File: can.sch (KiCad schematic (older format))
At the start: 13 parts, among them P7 CAN, U10 MCP2551-I/SN, U11 MCP2515, U12 SG-210STF_16MHz

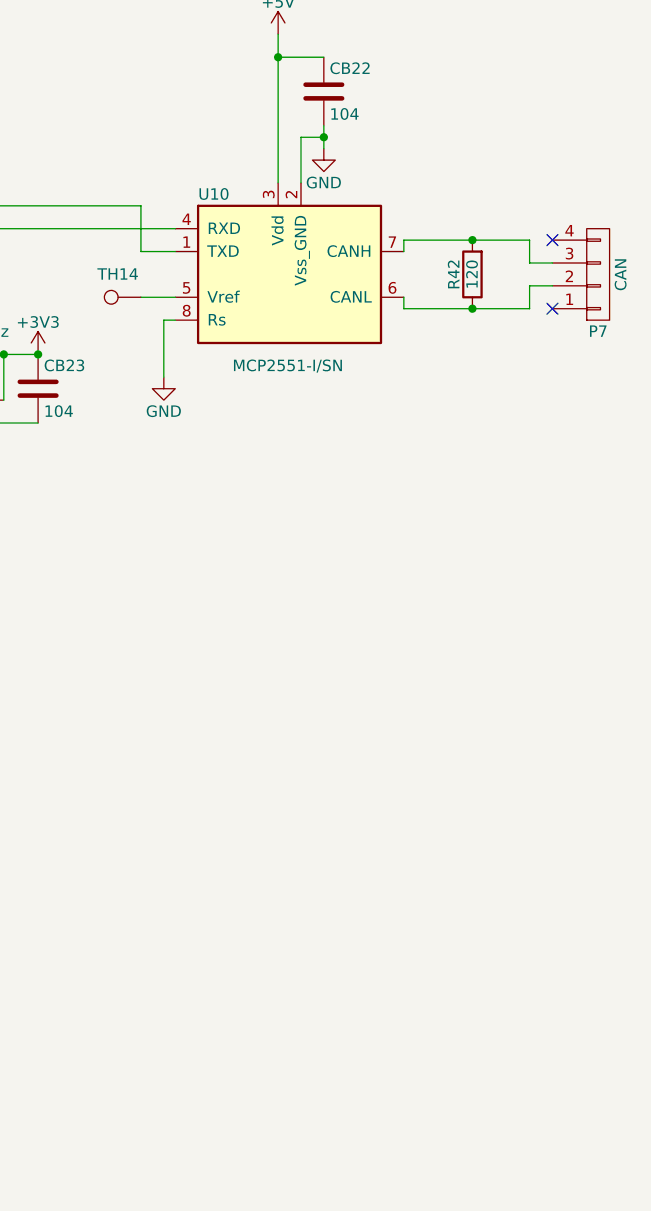
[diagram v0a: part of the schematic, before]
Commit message: Improved the pin comatibility to match with other ardupilot project.
Signed-off-by: Akira Tsukamoto <akira-t@s9.dion.ne.jp>
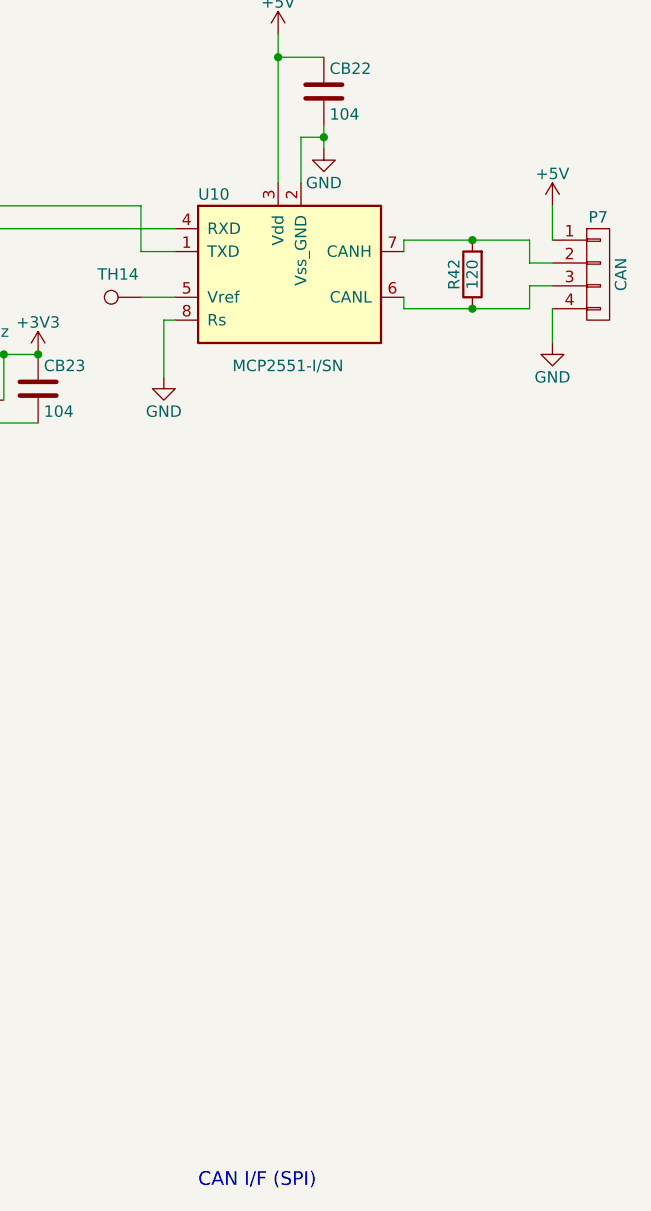
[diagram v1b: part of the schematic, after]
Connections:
- net +5V: now also P7.1 (P1)
- net GND: now also P7.4 (P4)
- net at R42.1, U10.6 (CANL): now also P7.3 (P3); no longer P7.2 (P2)
- net at R42.2, U10.7 (CANH): now also P7.2 (P2); no longer P7.3 (P3)
- no-connect marks 8 -> 6
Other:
- note added: "CAN I/F (SPI)"
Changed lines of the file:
@@
 F 3 "" H 9100 3500 60  0000 C CNN
 	1    9100 3500
-	1    0    0    1
+	1    0    0    -1
 $EndComp
 Wire Wire Line
@@
 Wire Wire Line
 	8800 3550 8800 3650
-NoConn ~ 8900 3350
-NoConn ~ 8900 3650
 Connection ~ 5500 4300
 Wire Wire Line
@@
 	1    0    0    -1
 $EndComp
+Text Notes 7350 7500 0    60   ~ 0
+CAN I/F (SPI)
+$Comp
+L +5V #PWR073
+U 1 1 5A32F9DD
+P 8900 3200
+F 0 "#PWR073" H 8900 3050 50  0001 C CNN
+F 1 "+5V" H 8900 3340 50  0000 C CNN
+F 2 "" H 8900 3200 50  0001 C CNN
+F 3 "" H 8900 3200 50  0001 C CNN
+	1    8900 3200
+	1    0    0    -1
+$EndComp
+$Comp
+L GND #PWR074
+U 1 1 5A32FADB
+P 8900 3800
+F 0 "#PWR074" H 8900 3550 50  0001 C CNN
+F 1 "GND" H 8900 3650 50  0000 C CNN
+F 2 "" H 8900 3800 50  0000 C CNN
+F 3 "" H 8900 3800 50  0000 C CNN
+	1    8900 3800
+	1    0    0    -1
+$EndComp
+Wire Wire Line
+	8900 3650 8900 3800
+Wire Wire Line
+	8900 3350 8900 3200
 $EndSCHEMATC
